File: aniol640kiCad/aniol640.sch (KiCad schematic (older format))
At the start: 32 parts, among them J1 RST, J2 PWR, U12 74LS74, U2 74LS14, U4 74LS32, U5 74LS08, U6 74LS02, X1 ACO-1.8432MHz

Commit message: created A640 kiCad chematic
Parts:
- removed RAM: HM62256BLP, Package_DIP:DIP-28_W15.24mm, symbol Memory_RAM:HM62256BLP
- removed ROM1: 28C256, Package_DIP:DIP-28_W15.24mm_Socket, symbol Memory_EEPROM:28C256
- removed U6: 74LS02, symbol 74xx:74LS02
- added R?: 4k7, symbol Device:R_Small
- added RN?: 4k7, Resistor_THT:R_Array_SIP9, symbol Device:R_Network08
- added U?: AS6C4008-55PCN, Package_DIP:DIP-32_W15.24mm, symbol Memory_RAM:AS6C4008-55PCN
- added U?: 27C010, symbol Memory_EPROM:27C010
- added U? (x2): 74LS32, symbol 74xx:74LS32
- added U?: 74LS573, symbol 74xx:74LS573
- added U? (x2): 74LS14, symbol 74xx:74LS14
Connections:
- net labels added: RAM_A14, RAM_A15, RAM_A16, RAM_A17, RAM_A18, ROM_A14, ROM_A15, ROM_A16, VRAMSEL'
- wire segments 86 -> 120
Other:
- moved on the sheet: J1, J2, R2, U?A, U?B, X1

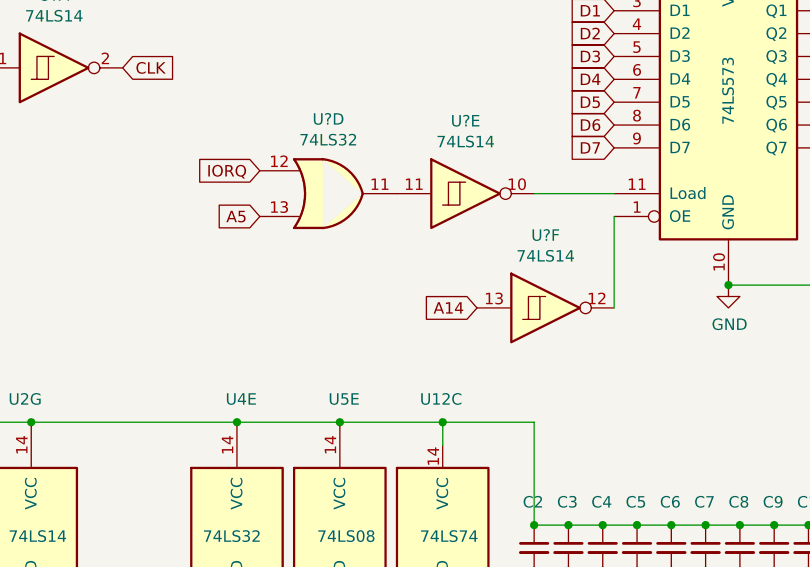
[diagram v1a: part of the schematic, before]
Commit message: fixes in keyboard schematic, writing procedures for the VGA card
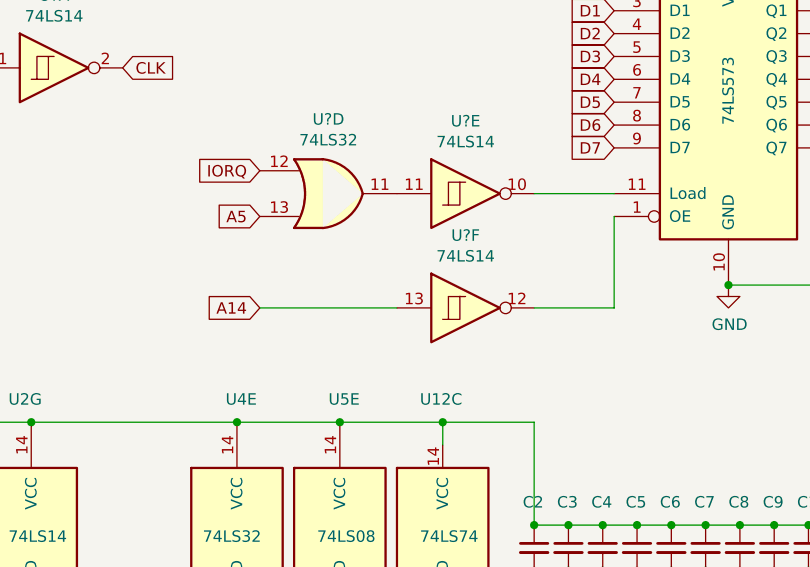
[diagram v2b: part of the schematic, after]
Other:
- moved on the sheet: U?F
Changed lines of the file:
@@
 	1    0    0    -1
 $EndComp
-Text GLabel 4050 6050 0    50   Input ~ 0
+Text GLabel 3100 6050 0    50   Input ~ 0
 A14
 $Comp
 L 74xx:74LS14 U?
 U 6 1 6253E7E7
-P 4350 6050
-F 0 "U?" H 4350 6367 50  0000 C CNN
-F 1 "74LS14" H 4350 6276 50  0000 C CNN
-F 2 "" H 4350 6050 50  0001 C CNN
-F 3 "http://www.ti.com/lit/gpn/sn74LS14" H 4350 6050 50  0001 C CNN
-	6    4350 6050
+P 4000 6050
+F 0 "U?" H 4000 6367 50  0000 C CNN
+F 1 "74LS14" H 4000 6276 50  0000 C CNN
+F 2 "" H 4000 6050 50  0001 C CNN
+F 3 "http://www.ti.com/lit/gpn/sn74LS14" H 4000 6050 50  0001 C CNN
+	6    4000 6050
 	1    0    0    -1
 $EndComp
@@
 Wire Wire Line
 	2100 7550 3000 7550
+Wire Wire Line
+	3100 6050 3700 6050
+Wire Wire Line
+	4300 6050 4650 6050
 $EndSCHEMATC

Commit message: developing the skbd module
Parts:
- added CR2032: 3V, symbol Device:Battery_Cell
- added D? (x2): D_Schottky, symbol Device:D_Schottky
- added R?: 4k7, symbol Device:R_Small
- gave numbers to parts that had none: 1
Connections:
- net +5V: now also D?.2 (A); no longer RAM.32 (VCC)
- net GND: now also RAM.16 (VSS), CR2032.2 (-)
- net RAMSEL: now also R?.2
- new net: D?.1 (K), D?.1 (K), R?.1, RAM.32 (VCC)
- new net: CR2032.1 (+), D?.2 (A)
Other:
- moved on the sheet: J1, J2, R2
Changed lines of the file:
@@
 L power:GND #PWR02
 U 1 1 61D165C5
-P 10000 2500
-F 0 "#PWR02" H 10000 2250 50  0001 C CNN
-F 1 "GND" H 10005 2327 50  0000 C CNN
-F 2 "" H 10000 2500 50  0001 C CNN
-F 3 "" H 10000 2500 50  0001 C CNN
-	1    10000 2500
+P 10200 4700
+F 0 "#PWR02" H 10200 4450 50  0001 C CNN
+F 1 "GND" H 10205 4527 50  0000 C CNN
+F 2 "" H 10200 4700 50  0001 C CNN
+F 3 "" H 10200 4700 50  0001 C CNN
+	1    10200 4700
 	1    0    0    -1
 $EndComp
@@
 L power:+5V #PWR01
 U 1 1 61D16900
-P 10000 1350
-F 0 "#PWR01" H 10000 1200 50  0001 C CNN
-F 1 "+5V" H 10015 1523 50  0000 C CNN
-F 2 "" H 10000 1350 50  0001 C CNN
-F 3 "" H 10000 1350 50  0001 C CNN
-	1    10000 1350
+P 10200 3550
+F 0 "#PWR01" H 10200 3400 50  0001 C CNN
+F 1 "+5V" H 10215 3723 50  0000 C CNN
+F 2 "" H 10200 3550 50  0001 C CNN
+F 3 "" H 10200 3550 50  0001 C CNN
+	1    10200 3550
 	1    0    0    -1
 $EndComp
@@
 L Device:R_Small R2
 U 1 1 61D1747F
-P 10000 1550
-F 0 "R2" H 10059 1596 50  0000 L CNN
-F 1 "4k7" H 10059 1505 50  0000 L CNN
-F 2 "Resistor_THT:R_Axial_DIN0207_L6.3mm_D2.5mm_P7.62mm_Horizontal" H 10000 1550 50  0001 C CNN
-F 3 "~" H 10000 1550 50  0001 C CNN
-	1    10000 1550
-	1    0    0    -1
-$EndComp
-Wire Wire Line
-	10000 1350 10000 1450
-Wire Wire Line
-	10000 1650 10000 1850
-Text GLabel 10200 1850 2    50   Input ~ 0
+P 10200 3750
+F 0 "R2" H 10259 3796 50  0000 L CNN
+F 1 "4k7" H 10259 3705 50  0000 L CNN
+F 2 "Resistor_THT:R_Axial_DIN0207_L6.3mm_D2.5mm_P7.62mm_Horizontal" H 10200 3750 50  0001 C CNN
+F 3 "~" H 10200 3750 50  0001 C CNN
+	1    10200 3750
+	1    0    0    -1
+$EndComp
+Wire Wire Line
+	10200 3550 10200 3650
+Wire Wire Line
+	10200 3850 10200 4050
+Text GLabel 10400 4050 2    50   Input ~ 0
 RST
 Wire Wire Line
-	10200 1850 10000 1850
-Connection ~ 10000 1850
+	10400 4050 10200 4050
+Connection ~ 10200 4050
 $Comp
 L 74xx:74LS08 U5
@@
 L Connector:Conn_01x02_Male J2
 U 1 1 61D552DF
-P 10550 2250
-F 0 "J2" H 10658 2431 50  0000 C CNN
-F 1 "PWR" H 10450 2200 50  0000 C CNN
-F 2 "Connector_PinHeader_2.54mm:PinHeader_1x02_P2.54mm_Vertical" H 10550 2250 50  0001 C CNN
-F 3 "~" H 10550 2250 50  0001 C CNN
-	1    10550 2250
+P 10750 4450
+F 0 "J2" H 10858 4631 50  0000 C CNN
+F 1 "PWR" H 10650 4400 50  0000 C CNN
+F 2 "Connector_PinHeader_2.54mm:PinHeader_1x02_P2.54mm_Vertical" H 10750 4450 50  0001 C CNN
+F 3 "~" H 10750 4450 50  0001 C CNN
+	1    10750 4450
 	1    0    0    -1
 $EndComp
@@
 L power:GND #PWR06
 U 1 1 61D56634
-P 10750 2350
-F 0 "#PWR06" H 10750 2100 50  0001 C CNN
-F 1 "GND" H 10755 2177 50  0000 C CNN
-F 2 "" H 10750 2350 50  0001 C CNN
-F 3 "" H 10750 2350 50  0001 C CNN
-	1    10750 2350
+P 10950 4550
+F 0 "#PWR06" H 10950 4300 50  0001 C CNN
+F 1 "GND" H 10955 4377 50  0000 C CNN
+F 2 "" H 10950 4550 50  0001 C CNN
+F 3 "" H 10950 4550 50  0001 C CNN
+	1    10950 4550
 	1    0    0    -1
 $EndComp
@@
 L power:+5V #PWR05
 U 1 1 61D56F4A
-P 10750 2250
-F 0 "#PWR05" H 10750 2100 50  0001 C CNN
-F 1 "+5V" H 10765 2423 50  0000 C CNN
-F 2 "" H 10750 2250 50  0001 C CNN
-F 3 "" H 10750 2250 50  0001 C CNN
-	1    10750 2250
+P 10950 4450
+F 0 "#PWR05" H 10950 4300 50  0001 C CNN
+F 1 "+5V" H 10965 4623 50  0000 C CNN
+F 2 "" H 10950 4450 50  0001 C CNN
+F 3 "" H 10950 4450 50  0001 C CNN
+	1    10950 4450
 	1    0    0    -1
 $EndComp
@@
 L Connector:Conn_01x02_Male J1
 U 1 1 61D57B45
-P 9800 2200
-F 0 "J1" H 9908 2381 50  0000 C CNN
-F 1 "RST" H 9700 2150 50  0000 C CNN
-F 2 "Connector_PinHeader_2.54mm:PinHeader_1x02_P2.54mm_Vertical" H 9800 2200 50  0001 C CNN
-F 3 "~" H 9800 2200 50  0001 C CNN
-	1    9800 2200
-	1    0    0    -1
-$EndComp
-Wire Wire Line
-	10000 1850 10000 2200
-Wire Wire Line
-	10000 2300 10000 2500
+P 10000 4400
+F 0 "J1" H 10108 4581 50  0000 C CNN
+F 1 "RST" H 9900 4350 50  0000 C CNN
+F 2 "Connector_PinHeader_2.54mm:PinHeader_1x02_P2.54mm_Vertical" H 10000 4400 50  0001 C CNN
+F 3 "~" H 10000 4400 50  0001 C CNN
+	1    10000 4400
+	1    0    0    -1
+$EndComp
+Wire Wire Line
+	10200 4050 10200 4400
+Wire Wire Line
+	10200 4500 10200 4700
 Wire Wire Line
 	2150 2200 2150 2800
@@
 L power:+5V #PWR?
 U 1 1 62297CAA
-P 8450 1750
-F 0 "#PWR?" H 8450 1600 50  0001 C CNN
-F 1 "+5V" H 8465 1923 50  0000 C CNN
-F 2 "" H 8450 1750 50  0001 C CNN
-F 3 "" H 8450 1750 50  0001 C CNN
-	1    8450 1750
+P 8450 1100
+F 0 "#PWR?" H 8450 950 50  0001 C CNN
+F 1 "+5V" H 8465 1273 50  0000 C CNN
+F 2 "" H 8450 1100 50  0001 C CNN
+F 3 "" H 8450 1100 50  0001 C CNN
+	1    8450 1100
 	1    0    0    -1
 $EndComp
@@
 L power:GND #PWR?
 U 1 1 622986B6
-P 8450 3900
-F 0 "#PWR?" H 8450 3650 50  0001 C CNN
-F 1 "GND" H 8455 3727 50  0000 C CNN
-F 2 "" H 8450 3900 50  0001 C CNN
-F 3 "" H 8450 3900 50  0001 C CNN
-	1    8450 3900
+P 8450 3950
+F 0 "#PWR?" H 8450 3700 50  0001 C CNN
+F 1 "GND" H 8455 3777 50  0000 C CNN
+F 2 "" H 8450 3950 50  0001 C CNN
+F 3 "" H 8450 3950 50  0001 C CNN
+	1    8450 3950
 	1    0    0    -1
 $EndComp
@@
 Text GLabel 6100 3550 0    50   Input ~ 0
 ROMSEL
-Text GLabel 8950 2950 2    50   Input ~ 0
+Text GLabel 9600 2950 2    50   Input ~ 0
 RAMSEL
 Text GLabel 7950 1950 0    50   Input ~ 0
@@
 ROMSEL
 $Comp
-L Memory_RAM:AS6C4008-55PCN U?
+L Memory_RAM:AS6C4008-55PCN RAM
 U 1 1 6248C2B7
 P 8450 2850
-F 0 "U?" H 8450 4131 50  0000 C CNN
+F 0 "RAM" H 8450 2350 50  0000 C CNN
 F 1 "AS6C4008-55PCN" V 8450 3000 50  0000 C CNN
 F 2 "Package_DIP:DIP-32_W15.24mm" H 8450 2950 50  0001 C CNN
@@
 Wire Wire Line
 	4300 6050 4650 6050
+$Comp
+L Device:D_Schottky D?
+U 1 1 625B1E53
+P 8450 1250
+F 0 "D?" V 8496 1170 50  0000 R CNN
+F 1 "D_Schottky" V 8405 1170 50  0000 R CNN
+F 2 "" H 8450 1250 50  0001 C CNN
+F 3 "~" H 8450 1250 50  0001 C CNN
+	1    8450 1250
+	0    -1   -1   0
+$EndComp
+$Comp
+L Device:D_Schottky D?
+U 1 1 625B23EB
+P 9550 1400
+F 0 "D?" H 9550 1617 50  0000 C CNN
+F 1 "D_Schottky" H 9550 1526 50  0000 C CNN
+F 2 "" H 9550 1400 50  0001 C CNN
+F 3 "~" H 9550 1400 50  0001 C CNN
+	1    9550 1400
+	1    0    0    -1
+$EndComp
+Wire Wire Line
+	8450 1400 8450 1750
+Connection ~ 8450 1400
+Wire Wire Line
+	8450 1400 9350 1400
+$Comp
+L Device:R_Small R?
+U 1 1 625D62BC
+P 9350 2200
+F 0 "R?" H 9409 2246 50  0000 L CNN
+F 1 "4k7" H 9409 2155 50  0000 L CNN
+F 2 "" H 9350 2200 50  0001 C CNN
+F 3 "~" H 9350 2200 50  0001 C CNN
+	1    9350 2200
+	1    0    0    -1
+$EndComp
+Wire Wire Line
+	9350 1400 9350 2100
+Connection ~ 9350 1400
+Wire Wire Line
+	9350 1400 9400 1400
+Wire Wire Line
+	9350 2300 9350 2950
+Wire Wire Line
+	9350 2950 8950 2950
+Wire Wire Line
+	9350 2950 9600 2950
+Connection ~ 9350 2950
+$Comp
+L Device:Battery_Cell CR2032
+U 1 1 625E844B
+P 10150 1650
+F 0 "CR2032" H 10268 1746 50  0000 L CNN
+F 1 "3V" H 10268 1655 50  0000 L CNN
+F 2 "" V 10150 1710 50  0001 C CNN
+F 3 "~" V 10150 1710 50  0001 C CNN
+	1    10150 1650
+	1    0    0    -1
+$EndComp
+Wire Wire Line
+	10150 1450 10150 1400
+Wire Wire Line
+	10150 1400 9700 1400
+$Comp
+L power:GND #PWR?
+U 1 1 625F0565
+P 10150 1750
+F 0 "#PWR?" H 10150 1500 50  0001 C CNN
+F 1 "GND" H 10155 1577 50  0000 C CNN
+F 2 "" H 10150 1750 50  0001 C CNN
+F 3 "" H 10150 1750 50  0001 C CNN
+	1    10150 1750
+	1    0    0    -1
+$EndComp
 $EndSCHEMATC

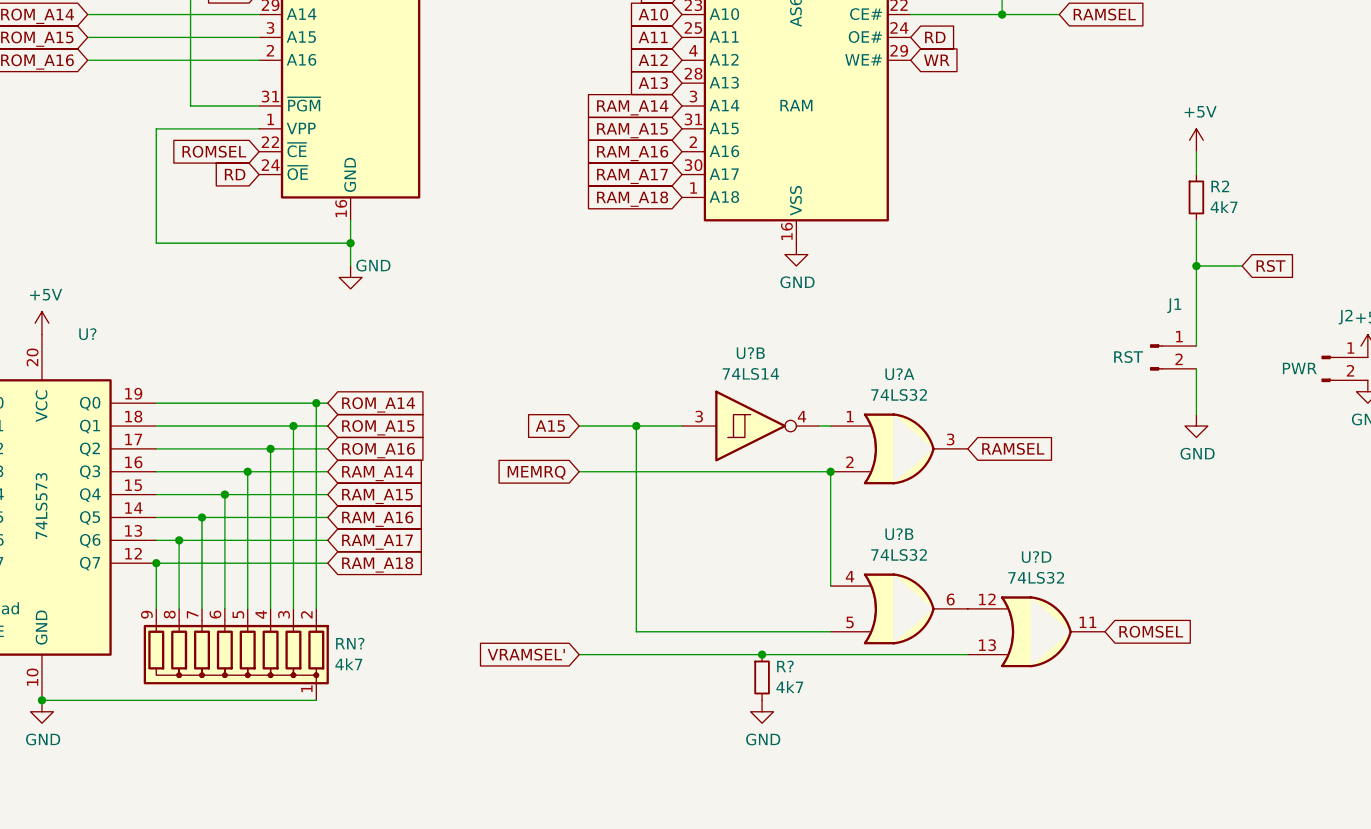
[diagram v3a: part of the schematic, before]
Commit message: Added basic PS2 keyboard support
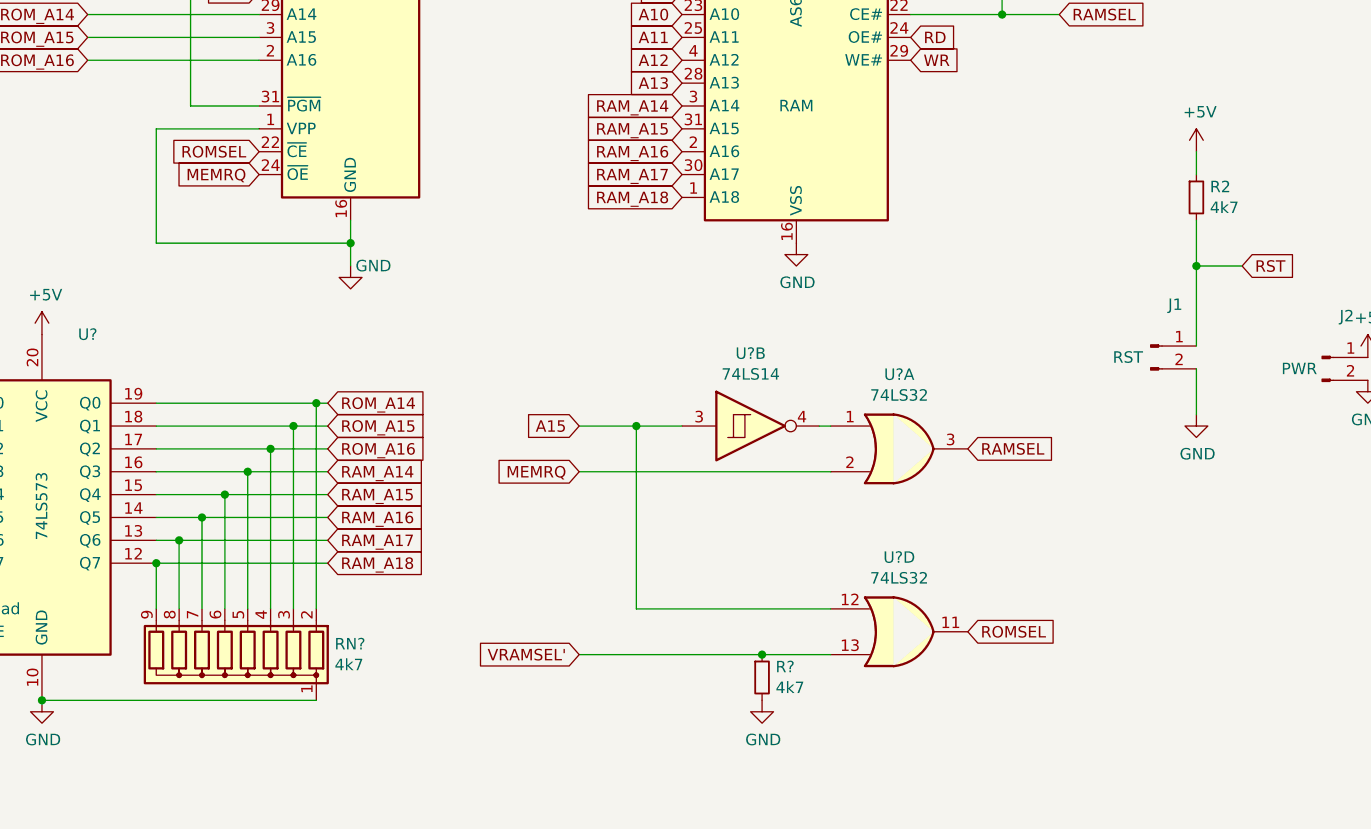
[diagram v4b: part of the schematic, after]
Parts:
- removed U?: 74LS32, symbol 74xx:74LS32
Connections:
- net A15: now also U?.12
- net MEMRQ: now also U?.24 (~OE)
- net RD: no longer U?.24 (~OE)
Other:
- moved on the sheet: U?D
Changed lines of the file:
@@
 WR
 Text GLabel 6100 3650 0    50   Input ~ 0
-RD
+MEMRQ
 Text GLabel 2900 1600 0    50   Input ~ 0
 RST
@@
 	1    0    0    -1
 $EndComp
-$Comp
-L 74xx:74LS32 U?
-U 2 1 62492E17
-P 8900 5550
-F 0 "U?" H 8900 5875 50  0000 C CNN
-F 1 "74LS32" H 8900 5784 50  0000 C CNN
-F 2 "" H 8900 5550 50  0001 C CNN
-F 3 "http://www.ti.com/lit/gpn/sn74LS32" H 8900 5550 50  0001 C CNN
-	2    8900 5550
-	1    0    0    -1
-$EndComp
 Text GLabel 7500 4750 0    50   Input ~ 0
 A15
 Wire Wire Line
 	7500 4750 7750 4750
-Wire Wire Line
-	8600 5650 7750 5650
-Wire Wire Line
-	7750 5650 7750 4750
 Connection ~ 7750 4750
 Wire Wire Line
 	7750 4750 7950 4750
 Wire Wire Line
-	8600 4950 8600 5450
-Wire Wire Line
 	8600 4750 8550 4750
 Wire Wire Line
 	8600 4950 7500 4950
-Connection ~ 8600 4950
 Text GLabel 7500 4950 0    50   Input ~ 0
 MEMRQ
 Text GLabel 9200 4850 2    50   Input ~ 0
 RAMSEL
-Text GLabel 9800 5650 2    50   Input ~ 0
+Text GLabel 9200 5650 2    50   Input ~ 0
 ROMSEL
 $Comp
@@
 L 74xx:74LS32 U?
 U 4 1 6249C96C
-P 9500 5650
-F 0 "U?" H 9500 5975 50  0000 C CNN
-F 1 "74LS32" H 9500 5884 50  0000 C CNN
-F 2 "" H 9500 5650 50  0001 C CNN
-F 3 "http://www.ti.com/lit/gpn/sn74LS32" H 9500 5650 50  0001 C CNN
-	4    9500 5650
-	1    0    0    -1
-$EndComp
-Wire Wire Line
-	9200 5750 8300 5750
+P 8900 5650
+F 0 "U?" H 8900 5975 50  0000 C CNN
+F 1 "74LS32" H 8900 5884 50  0000 C CNN
+F 2 "" H 8900 5650 50  0001 C CNN
+F 3 "http://www.ti.com/lit/gpn/sn74LS32" H 8900 5650 50  0001 C CNN
+	4    8900 5650
+	1    0    0    -1
+$EndComp
 Text GLabel 7500 5750 0    50   Input ~ 0
 VRAMSEL'
@@
 	1    0    0    -1
 $EndComp
-Connection ~ 8300 5750
 Wire Wire Line
 	8300 5750 7500 5750
@@
 	1    0    0    -1
 $EndComp
+Wire Wire Line
+	8600 5750 8300 5750
+Connection ~ 8300 5750
+Wire Wire Line
+	8600 5550 7750 5550
+Wire Wire Line
+	7750 4750 7750 5550
 $EndSCHEMATC
